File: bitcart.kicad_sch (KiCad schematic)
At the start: 0 parts

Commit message: added a lot more parts
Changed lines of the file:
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@@
     (stroke (width 0) (type default))
   )
-  (wire (pts (xy 66.675 67.31) (xy 74.295 67.31))
+  (wire (pts (xy 101.346 121.666) (xy 108.966 121.666))
     (stroke (width 0) (type solid))
   )
@@
     (stroke (width 0) (type default))
   )
-  (wire (pts (xy 66.675 71.12) (xy 74.295 71.12))
+  (wire (pts (xy 101.346 125.476) (xy 108.966 125.476))
     (stroke (width 0) (type solid))
   )
@@
     (effects (font (size 1.27 1.27)) (justify left bottom))
   )
-  (label "+5v" (at 69.215 71.12 0) (fields_autoplaced)
+  (label "+5v" (at 103.886 125.476 0) (fields_autoplaced)
     (effects (font (size 1.27 1.27)) (justify left bottom))
   )
@@
     (effects (font (size 1.27 1.27)) (justify left bottom))
   )
-  (label "+12v" (at 69.215 67.31 0) (fields_autoplaced)
+  (label "+12v" (at 103.886 121.666 0) (fields_autoplaced)
     (effects (font (size 1.27 1.27)) (justify left bottom))
   )
@@
     )
   )
-  (sheet (at 38.735 59.69) (size 27.94 20.32)
+  (sheet (at 76.962 114.046) (size 24.384 20.32)
     (stroke (width 0.1524) (type solid))
     (fill (color 255 255 194 1.0000))
-    (property "Sheetname" "PSUs" (at 38.735 59.0545 0)
+    (property "Sheetname" "PSUs" (at 76.962 113.4105 0)
       (effects (font (size 1.27 1.27)) (justify left bottom))
     )
-    (property "Sheetfile" "PSUs.kicad_sch" (at 38.735 81.28 0)
+    (property "Sheetfile" "PSUs.kicad_sch" (at 76.962 135.636 0)
       (effects (font (size 1.27 1.27)) (justify left top))
     )
-    (pin "+5v" output (at 66.675 71.12 0)
-      (effects (font (size 1.27 1.27)) (justify right))
-    )
-    (pin "+12v" output (at 66.675 67.31 0)
-      (effects (font (size 1.27 1.27)) (justify right))
-    )
+    (pin "+5v" output (at 101.346 125.476 0)
+      (effects (font (size 1.27 1.27)) (justify right))
+    )
+    (pin "+12v" output (at 101.346 121.666 0)
+      (effects (font (size 1.27 1.27)) (justify right))
+    )

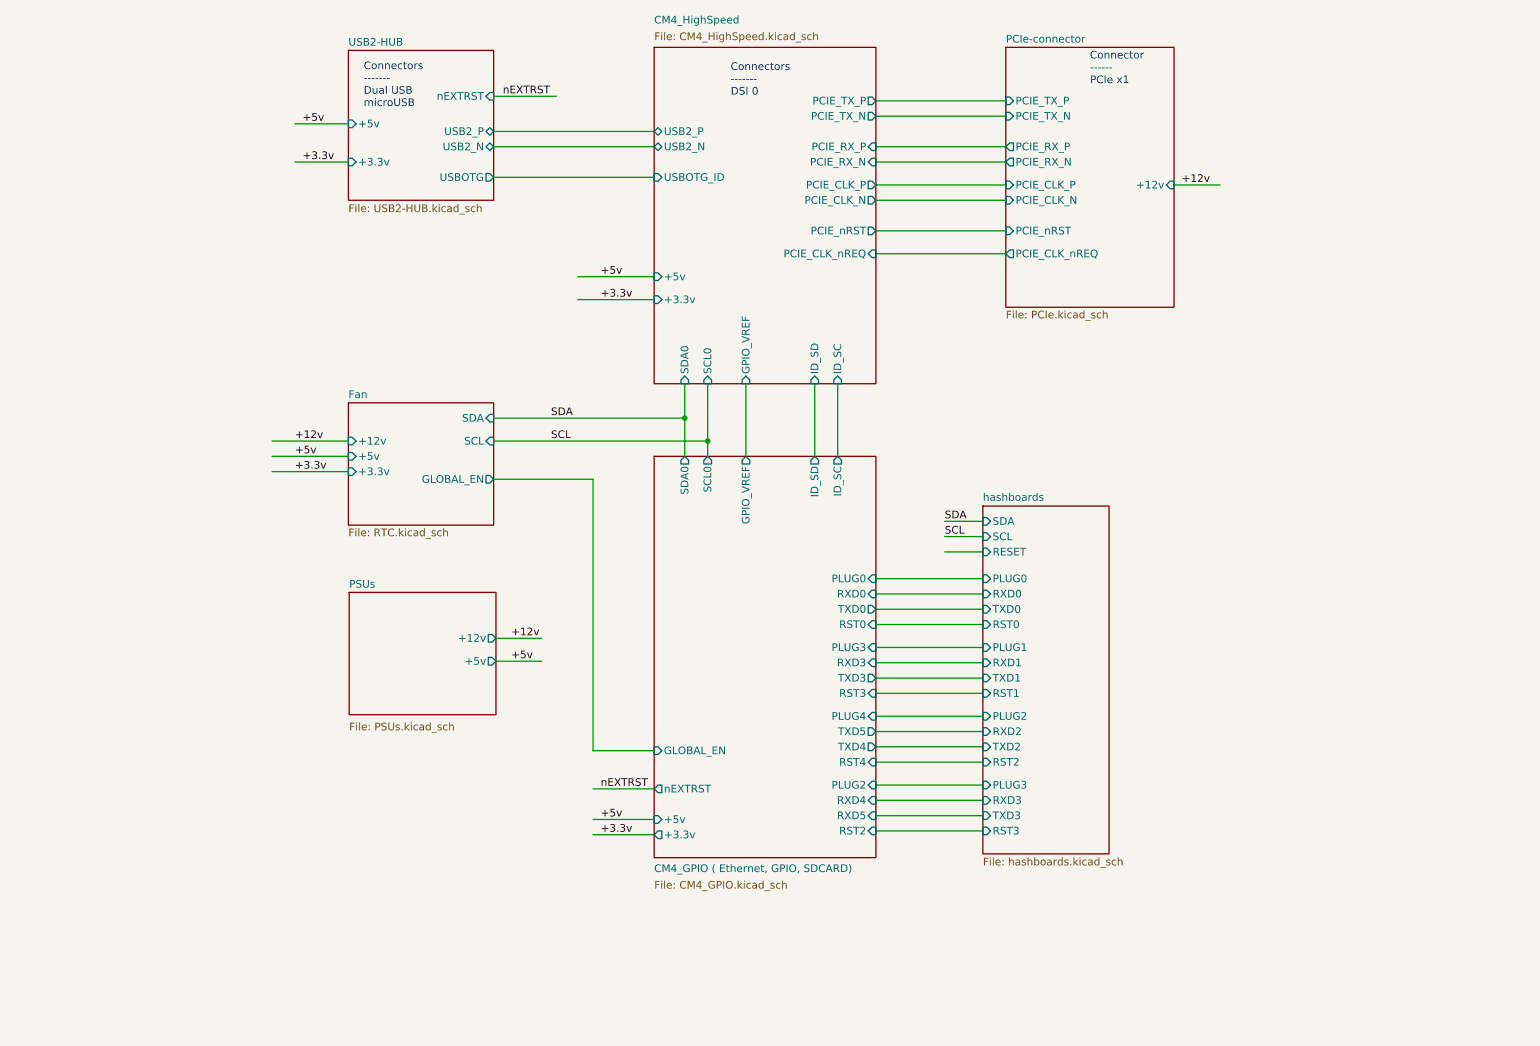
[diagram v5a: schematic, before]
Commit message: resolved some schematic-board errors. switched to tap-on-top ethernet.
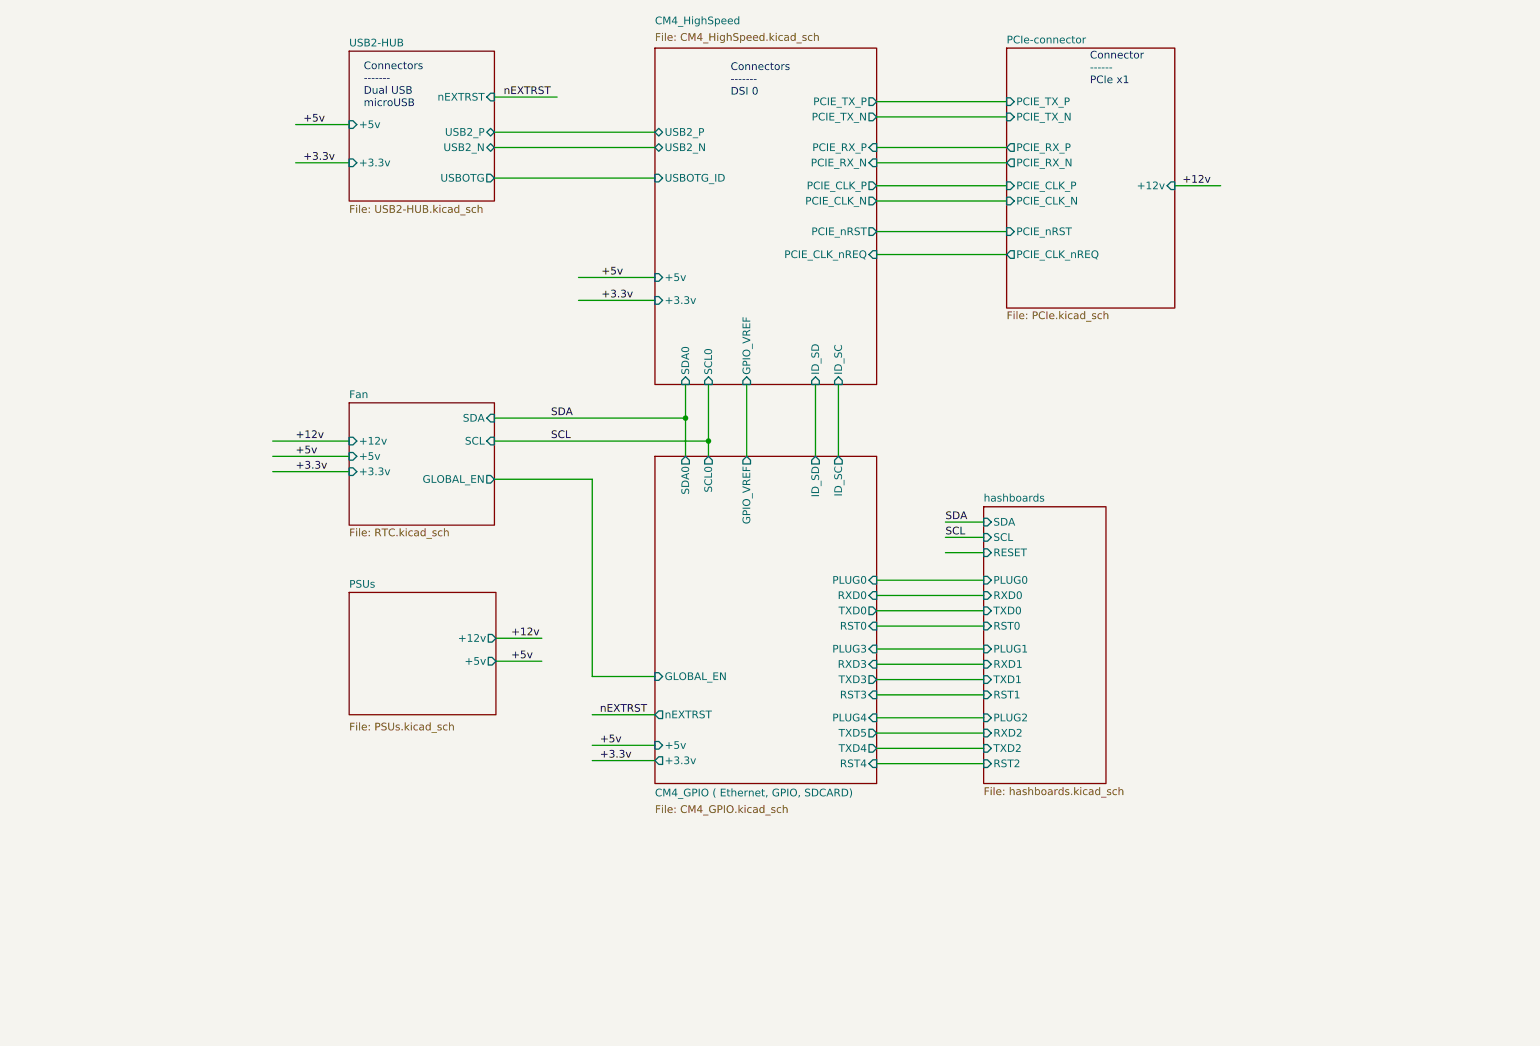
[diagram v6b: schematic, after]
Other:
- sheet CM4_GPIO ( Ethernet, GPIO, SDCARD) ports: added none; removed PLUG2, RST2, RXD4, RXD5
- sheet hashboards ports: added none; removed PLUG3, RST3, RXD3, TXD3

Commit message: pulled in bitcrane fan and data connectors and edge cuts. most placement done. started routing
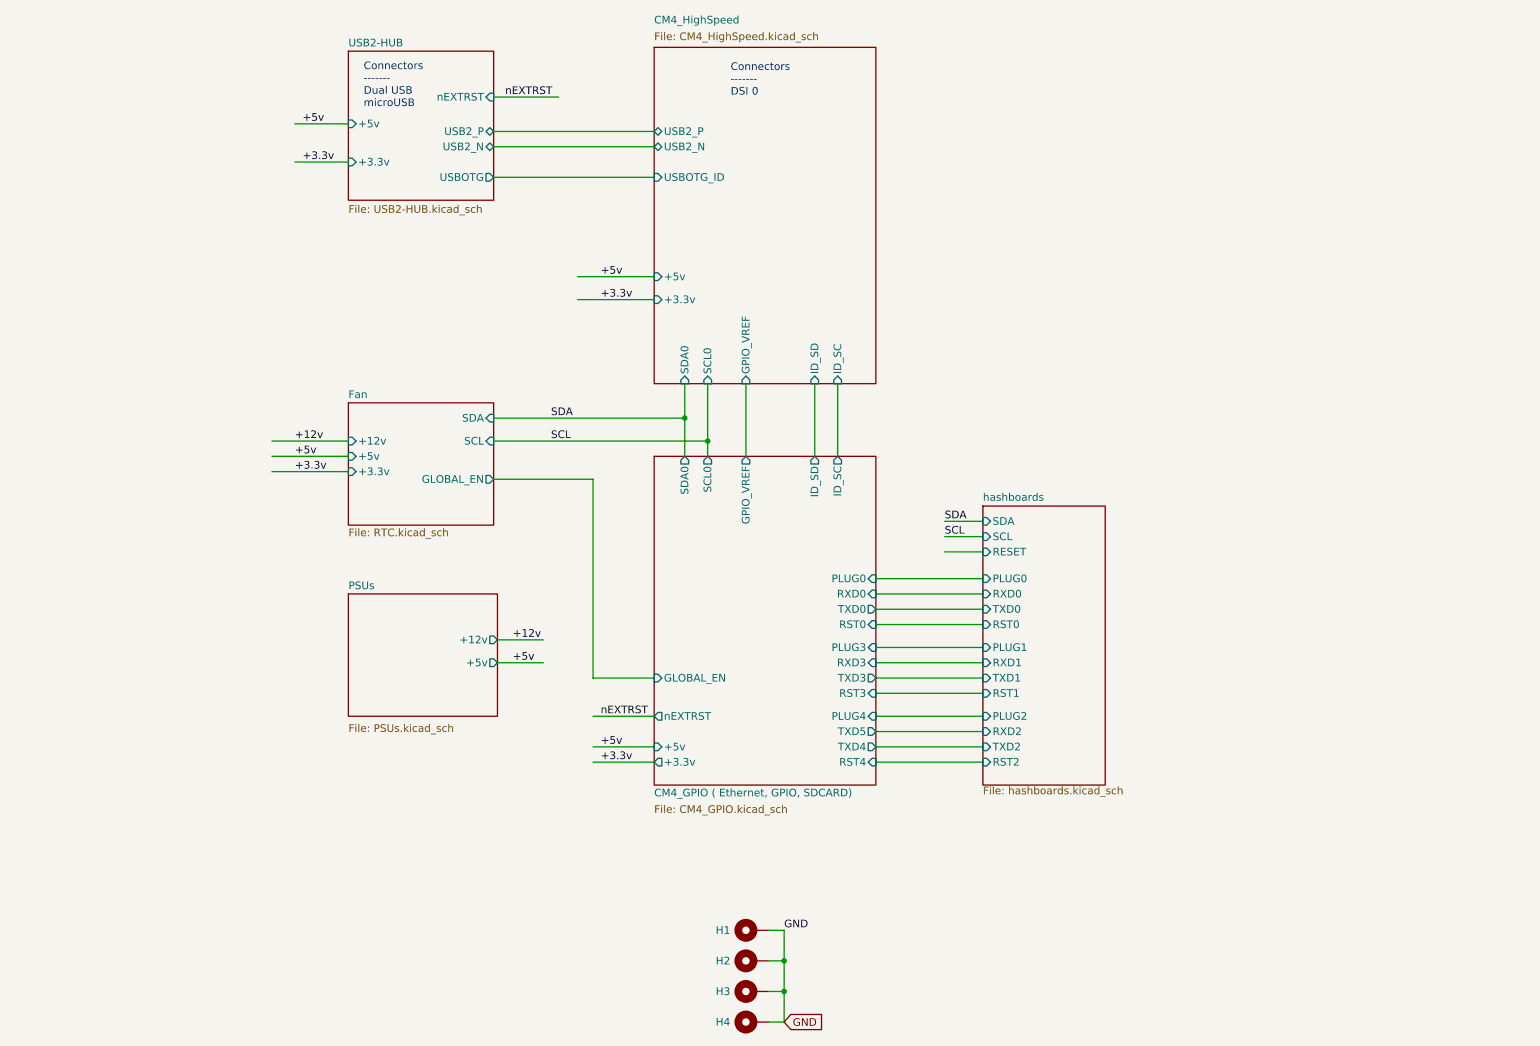
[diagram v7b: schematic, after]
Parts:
- added H1, H2, H3, H4: MountingHole_Pad, bitcrane:MountingHole_3mm_Pad, symbol Mechanical:MountingHole_Pad
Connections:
- new net GND: H1.1, H2.1, H3.1, H4.1
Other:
- removed sheet PCIe-connector
- sheet CM4_HighSpeed ports: added none; removed PCIE_CLK_N, PCIE_CLK_P, PCIE_CLK_nREQ, PCIE_RX_N, PCIE_RX_P, PCIE_TX_N, PCIE_TX_P, PCIE_nRST
- note removed: "Connector ------ PCIe x1"

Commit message: more placement
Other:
- sheet Fan ports: added none; removed +5v
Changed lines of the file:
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@@
-    (stroke (width 0) (type solid))
-  )
-  (wire (pts (xy 64.135 91.44) (xy 76.835 91.44))
     (stroke (width 0) (type solid))
   )
@@
   )
   (label "SCL" (at 175.895 104.775 0) (fields_autoplaced)
-    (effects (font (size 1.27 1.27)) (justify left bottom))
-  )
-  (label "+5v" (at 67.945 91.44 0) (fields_autoplaced)
     (effects (font (size 1.27 1.27)) (justify left bottom))
   )
@@
       (effects (font (size 1.27 1.27)) (justify right))
     )
-    (pin "+5v" input (at 76.835 91.44 180)
-      (effects (font (size 1.27 1.27)) (justify left))
-    )
     (pin "+3.3v" input (at 76.835 93.98 180)
